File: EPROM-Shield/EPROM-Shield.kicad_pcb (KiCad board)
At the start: 2 copper layers, 61 x 54.6 mm, 21 parts, among them J1 Conn_01x07, J2 Conn_01x06, J3 Conn_01x08, J4 Conn_01x06, U1 74LS595, U2 74LS595, U3 28C256

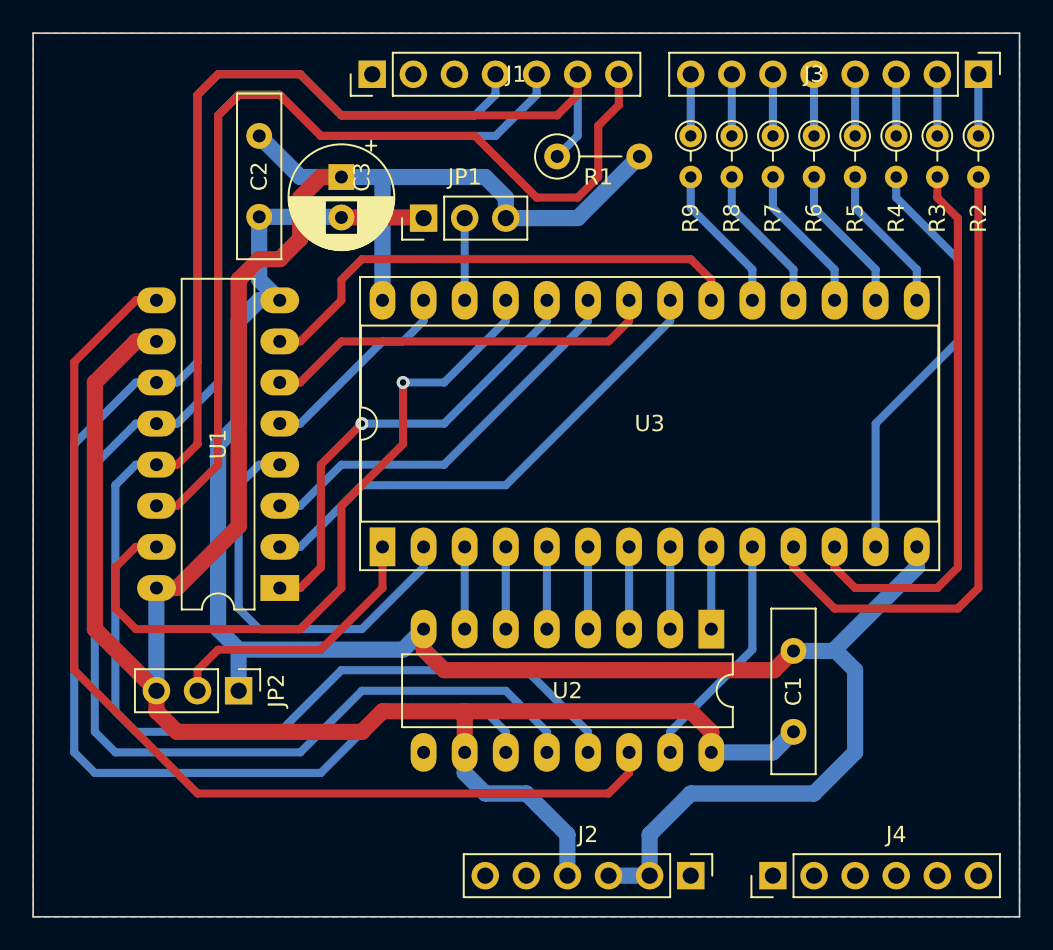
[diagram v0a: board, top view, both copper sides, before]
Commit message: EPROM-Shield
- D0/D1 can optionally be connected to AD0/AD1 (because D0/D1 are used for serial port on some Arduino boards)
- connected GND on D8-D13 connector
- fix C3 footprint
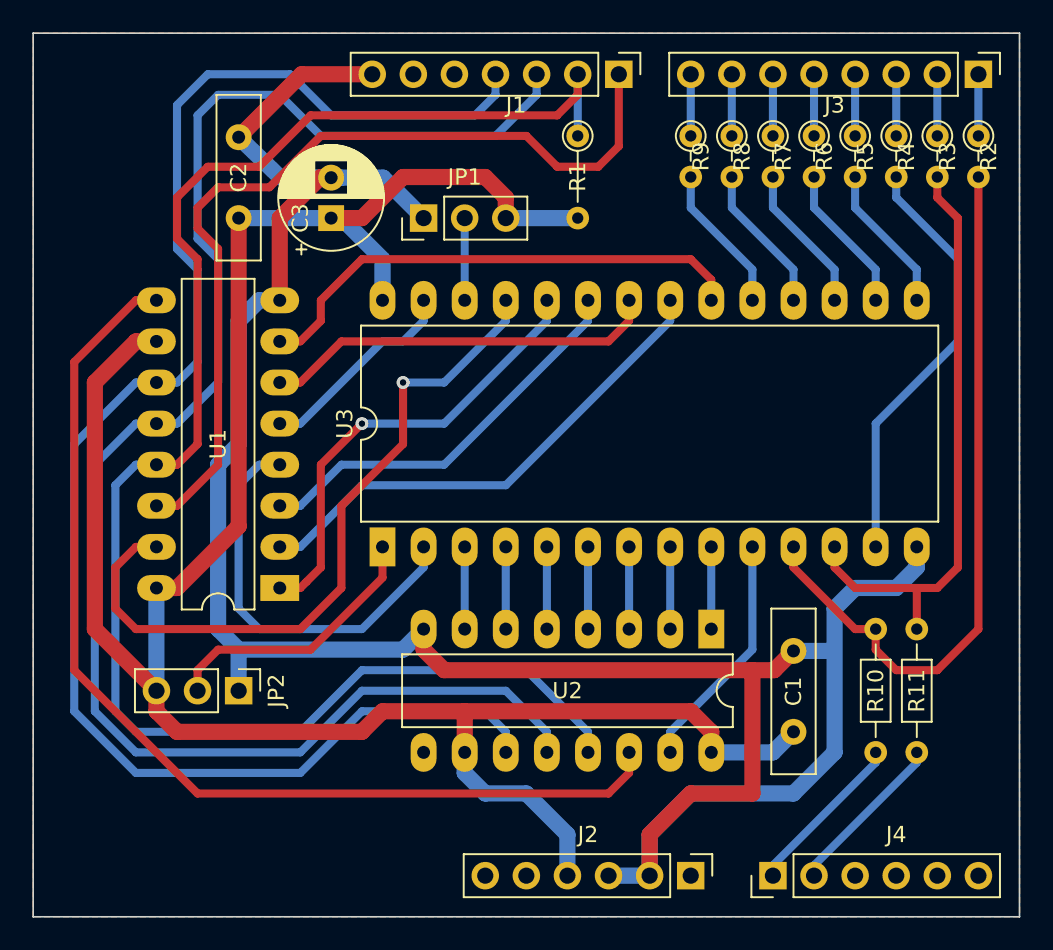
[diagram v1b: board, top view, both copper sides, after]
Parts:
- added R10: 510, Resistor_THT:R_Axial_DIN0204_L3.6mm_D1.6mm_P7.62mm_Horizontal, F.Cu at (138.4, 113.0)
- added R11: 510, Resistor_THT:R_Axial_DIN0204_L3.6mm_D1.6mm_P7.62mm_Horizontal, F.Cu at (141.0, 113.0)
- J1: value Conn_01x07 -> D8-D13
- J3: value Conn_01x08 -> D0-D7
- J4: value Conn_01x06 -> A0-A5
- R1: footprint Resistor_THT:R_Axial_DIN0207_L6.3mm_D2.5mm_P5.08mm_Vertical -> Resistor_THT:R_Axial_DIN0204_L3.6mm_D1.6mm_P5.08mm_Vertical
- U3: footprint Package_DIP:DIP-28_W15.24mm_Socket_LongPads -> Package_DIP:DIP-28_W15.24mm_LongPads
- moved J1 15.2 mm to (122.6, 71.1), turned to 270 degrees
- moved C2 5.24 mm to (99.1, 80.0), turned to 90 degrees
- moved C3 2.62 mm to (104.8, 80.0), turned to 90 degrees
- moved R1 1.80 mm to (120.0, 74.9), turned to 270 degrees
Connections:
- J1 pad 1: Net-(J1-Pad1) -> /SER
- J1 pad 2: Net-(J1-Pad2) -> /_OE
- J1 pad 3: Net-(J1-Pad3) -> /RCLK
- J1 pad 5: /RCLK -> (no net)
- J1 pad 6: /_OE -> (no net)
- J1 pad 7: /SER -> GND
- J2 pad 1: Net-(J2-Pad1) -> (no net)
- J2 pad 5: Net-(J2-Pad5) -> (no net)
- J2 pad 6: Net-(J2-Pad6) -> (no net)
- J4 pad 1: Net-(J4-Pad1) -> /AD0
- J4 pad 2: Net-(J4-Pad2) -> /AD1
- J4 pad 3: Net-(J4-Pad3) -> (no net)
- J4 pad 4: Net-(J4-Pad4) -> (no net)
- J4 pad 5: Net-(J4-Pad5) -> (no net)
- J4 pad 6: Net-(J4-Pad6) -> (no net)
- U2 pad 9: Net-(U2-Pad9) -> (no net)
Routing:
- net GND: track 117.7 -> 151.7 mm
- net VCC: track 158.0 -> 146.4 mm
- net /AD1: track 0.00 -> 10.3 mm
- net /AD0: track 0.00 -> 10.3 mm
- net /_OE: track 108.3 -> 102.5 mm
- net /SER: track 60.5 -> 54.9 mm
- net Net-(R10-Pad2): track 39.7 -> 45.1 mm
- net Net-(R11-Pad2): track 34.6 -> 37.1 mm
- net /RCLK: track 98.7 -> 99.7 mm
